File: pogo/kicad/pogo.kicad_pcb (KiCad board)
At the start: 2 copper layers, 7.6 x 15.1 mm, 6 parts

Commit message: Tweaked the layout.
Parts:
- added REF**: SolderJumper, pogo:SolderJumper, F.Cu at (0.00, 3.56)
- moved REF** 2.54 mm to (2.54, 0.00)
- moved REF** 2.54 mm to (0.00, 7.82)
- moved REF** 2.54 mm to (0.00, 0.00)
- moved REF** 2.54 mm to (-2.54, 0.00)
- moved REF** 2.54 mm to (0.00, -2.54)
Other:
- board size 7.6 x 15.1 mm -> 7.9 x 14.9 mm
- board text added: "+"
- board text added: "GND"
- board text added: "POGO PINS THIS SIDE"
- board text added: "SCL"
- board text added: "SDA"
- board text added: "SH 1MM SMD"
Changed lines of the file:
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@@
   (net 0 "")
   (footprint "pogo:POGO_PAD2" (layer "F.Cu")
-    (at 5.08 0)
+    (at 2.54 0)
     (descr "Through hole straight pin header, 1x01, 2.54mm pitch, single row")
     (tags "Through hole pin header THT 1x01 2.54mm single row")
@@
   )
   (footprint "pogo:JST_SH_SM04B-SRSS-TB_1x04-1MP_P1.00mm_Horizontal" (layer "F.Cu")
-    (at 2.54 7.8232)
+    (at 0 7.8232)
     (descr "JST SH series connector, SM04B-SRSS-TB (http://www.jst-mfg.com/product/pdf/eng/eSH.pdf), generated with kicad-footprint-generator")
     (tags "connector JST SH top entry")
@@
   )
   (footprint "pogo:POGO_PAD2" (layer "F.Cu")
-    (at 2.54 0)
+    (at 0 0)
     (descr "Through hole straight pin header, 1x01, 2.54mm pitch, single row")
     (tags "Through hole pin header THT 1x01 2.54mm single row")
@@
   )
   (footprint "pogo:POGO_PAD2" (layer "F.Cu")
-    (at 0 0)
+    (at -2.54 0)
     (descr "Through hole straight pin header, 1x01, 2.54mm pitch, single row")
     (tags "Through hole pin header THT 1x01 2.54mm single row")
@@
     )
   )
-  (footprint "pogo:POGO_PAD2" (layer "F.Cu")
-    (at 2.54 -2.54)
+  (footprint "pogo:SolderJumper" (layer "F.Cu")
+    (at 0 3.556)
+    (descr "SMD Solder Jumper, 1x1.5mm Pads, 0.3mm gap, open")
+    (tags "solder jumper open")
+    (attr exclude_from_pos_files exclude_from_bom)
+    (fp_text reference "REF**" (at 0 -1.8) (layer "F.SilkS") hide
+        (effects (font (size 1 1) (thickness 0.15)))
+    )
+    (fp_text value "SolderJumper" (at 0 1.9) (layer "F.Fab") hide
+        (effects (font (size 1 1) (thickness 0.15)))
+    )
+    (fp_line (start -1.4 -1) (end 1.4 -1)
+      (stroke (width 0.12) (type solid)) (layer "F.SilkS"))
+    (fp_line (start -1.4 1) (end -1.4 -1)
+      (stroke (width 0.12) (type solid)) (layer "F.SilkS"))
+    (fp_line (start 1.4 -1) (end 1.4 1)
+      (stroke (width 0.12) (type solid)) (layer "F.SilkS"))
+    (fp_line (start 1.4 1) (end -1.4 1)
+      (stroke (width 0.12) (type solid)) (layer "F.SilkS"))
+    (pad "1" smd rect (at -0.65 0) (size 1 1.5) (layers "F.Cu" "F.Mask"))
+    (pad "2" smd rect (at 0.65 0) (size 1 1.5) (layers "F.Cu" "F.Mask"))
+  )
+  (footprint "pogo:POGO_PAD2" (layer "F.Cu")
+    (at 0 -2.54)
     (descr "Through hole straight pin header, 1x01, 2.54mm pitch, single row")
     (tags "Through hole pin header THT 1x01 2.54mm single row")
@@
     )
   )
-  (gr_circle (center 0 0) (end 1.27 0)
-    (stroke (width 0.0254) (type default)) (fill none) (layer "F.SilkS"))
-  (gr_circle (center 5.08 0) (end 6.35 0)
-    (stroke (width 0.0254) (type default)) (fill none) (layer "F.SilkS"))
-  (gr_circle (center 2.54 -2.54) (end 3.81 -2.54)
-    (stroke (width 0.0254) (type default)) (fill none) (layer "F.SilkS"))
-  (gr_line (start 6.35 10.7188) (end 6.35 -0.5334)
-    (stroke (width 0.0254) (type default)) (layer "Edge.Cuts"))
-  (gr_line (start 6.35 -0.5334) (end 2.54 -4.3434)
-    (stroke (width 0.0254) (type default)) (layer "Edge.Cuts"))
-  (gr_line (start -1.27 10.7188) (end -1.27 -0.5334)
-    (stroke (width 0.0254) (type default)) (layer "Edge.Cuts"))
-  (gr_line (start -1.27 -0.5334) (end 2.54 -4.3434)
-    (stroke (width 0.0254) (type default)) (layer "Edge.Cuts"))
-  (gr_line (start -1.27 10.7188) (end 6.35 10.7188)
-    (stroke (width 0.0254) (type default)) (layer "Edge.Cuts"))
-  (segment (start 3.81 2.5654) (end 2.04 4.3354) (width 0.4064) (layer "F.Cu") (net 0))
-  (segment (start 2.04 4.3354) (end 2.04 5.62) (width 0.4064) (layer "F.Cu") (net 0))
-  (segment (start 4.04 5.62) (end 4.04 4.0626) (width 0.254) (layer "F.Cu") (net 0))
-  (segment (start 4.04 4.0626) (end 5.08 3.0226) (width 0.254) (layer "F.Cu") (net 0))
-  (segment (start 3.048 5.8312) (end 3.048 6.858) (width 0.254) (layer "F.Cu") (net 0))
-  (segment (start 3.81 2.5654) (end 3.81 -1.27) (width 0.4064) (layer "F.Cu") (net 0))
-  (segment (start 3.81 -1.27) (end 2.54 -2.54) (width 0.4064) (layer "F.Cu") (net 0))
-  (segment (start 0 6.7564) (end 0 0) (width 0.254) (layer "F.Cu") (net 0))
-  (segment (start 1.04 5.62) (end 1.04 1.5762) (width 0.4064) (layer "F.Cu") (net 0))
-  (segment (start 3.048 6.8834) (end 2.6162 7.3152) (width 0.254) (layer "F.Cu") (net 0))
-  (segment (start 5.08 3.0226) (end 5.08 0) (width 0.254) (layer "F.Cu") (net 0))
-  (segment (start 2.6162 7.3152) (end 0.5588 7.3152) (width 0.254) (layer "F.Cu") (net 0))
-  (segment (start 1.04 1.5762) (end 2.54 0.0762) (width 0.4064) (layer "F.Cu") (net 0))
-  (segment (start 0.5588 7.3152) (end 0 6.7564) (width 0.254) (layer "F.Cu") (net 0))
-  (segment (start 2.54 0.0762) (end 2.54 0) (width 0.4064) (layer "F.Cu") (net 0))
+  (gr_line (start 3.937 10.287) (end 3.937 -0.056344)
+    (stroke (width 0.0254) (type default)) (layer "Edge.Cuts"))
+  (gr_line (start 3.527828 -1.044172) (end 0.987828 -3.584172)
+    (stroke (width 0.0254) (type default)) (layer "Edge.Cuts"))
+  (gr_arc (start 3.937 10.287) (mid 3.751013 10.736013) (end 3.302 10.922)
+    (stroke (width 0.0254) (type default)) (layer "Edge.Cuts"))
+  (gr_arc (start -0.987828 -3.584172) (mid 0 -3.993344) (end 0.987828 -3.584172)
+    (stroke (width 0.0254) (type default)) (layer "Edge.Cuts"))
+  (gr_line (start -3.937 10.287) (end -3.937 -0.056344)
+    (stroke (width 0.0254) (type default)) (layer "Edge.Cuts"))
+  (gr_arc (start 3.527828 -1.044172) (mid 3.830659 -0.590953) (end 3.937 -0.056344)
+    (stroke (width 0.0254) (type default)) (layer "Edge.Cuts"))
+  (gr_arc (start -3.937 -0.056344) (mid -3.83066 -0.590953) (end -3.527828 -1.044172)
+    (stroke (width 0.0254) (type default)) (layer "Edge.Cuts"))
+  (gr_line (start -3.527828 -1.044172) (end -0.987828 -3.584172)
+    (stroke (width 0.0254) (type default)) (layer "Edge.Cuts"))
+  (gr_arc (start -3.302 10.922) (mid -3.751013 10.736013) (end -3.937 10.287)
+    (stroke (width 0.0254) (type default)) (layer "Edge.Cuts"))
+  (gr_line (start -3.302 10.922) (end 3.302 10.922)
+    (stroke (width 0.0254) (type default)) (layer "Edge.Cuts"))
+  (gr_text "POGO PINS\nTHIS SIDE" (at 0 2.413) (layer "B.SilkS")
+    (effects (font (size 0.75 0.75) (thickness 0.15)) (justify top mirror))
+  )
+  (gr_text "SCL" (at 2.54 1.016) (layer "F.SilkS")
+    (effects (font (size 0.75 0.75) (thickness 0.15)) (justify top))
+  )
+  (gr_text "+" (at -1.27 -2.667) (layer "F.SilkS")
+    (effects (font (size 0.75 0.75) (thickness 0.15)) (justify top))
+  )
+  (gr_text "GND" (at 0 1.016) (layer "F.SilkS")
+    (effects (font (size 0.75 0.75) (thickness 0.15)) (justify top))
+  )
+  (gr_text "SH 1MM\nSMD" (at 0 7.239) (layer "F.SilkS")
+    (effects (font (size 0.75 0.75) (thickness 0.15)) (justify top))
+  )
+  (gr_text "SDA" (at -2.54 1.016) (layer "F.SilkS")
+    (effects (font (size 0.75 0.75) (thickness 0.15)) (justify top))
+  )
+  (segment (start 0.65 1.763) (end 1.27 1.143) (width 0.4064) (layer "F.Cu") (net 0))
+  (segment (start 1.27 1.143) (end 1.27 -1.27) (width 0.4064) (layer "F.Cu") (net 0))
+  (segment (start 0.508 6.8834) (end -0.1016 7.493) (width 0.254) (layer "F.Cu") (net 0))
+  (segment (start -0.65 3.175) (end -0.5 3.325) (width 0.4064) (layer "F.Cu") (net 0))
+  (segment (start -2.794 6.731) (end -2.794 1.651) (width 0.254) (layer "F.Cu") (net 0))
+  (segment (start -0.5 3.325) (end -0.5 5.62) (width 0.4064) (layer "F.Cu") (net 0))
+  (segment (start 0.508 5.8312) (end 0.508 6.858) (width 0.254) (layer "F.Cu") (net 0))
+  (segment (start -2.032 7.493) (end -2.794 6.731) (width 0.254) (layer "F.Cu") (net 0))
+  (segment (start 0.65 3.175) (end 0.65 1.763) (width 0.4064) (layer "F.Cu") (net 0))
+  (segment (start -2.54 1.397) (end -2.54 0) (width 0.254) (layer "F.Cu") (net 0))
+  (segment (start 1.27 -1.27) (end 0 -2.54) (width 0.4064) (layer "F.Cu") (net 0))
+  (segment (start -2.794 1.651) (end -2.54 1.397) (width 0.254) (layer "F.Cu") (net 0))
+  (segment (start -1.5 5.62) (end -1.5 4.85) (width 0.4064) (layer "F.Cu") (net 0))
+  (segment (start -1.905 4.445) (end -1.905 1.905) (width 0.4064) (layer "F.Cu") (net 0))
+  (segment (start 2.54 3.81) (end 2.54 0) (width 0.254) (layer "F.Cu") (net 0))
+  (segment (start -1.5 4.85) (end -1.905 4.445) (width 0.4064) (layer "F.Cu") (net 0))
+  (segment (start -0.1016 7.493) (end -2.032 7.493) (width 0.254) (layer "F.Cu") (net 0))
+  (segment (start 1.5 5.62) (end 1.5 4.85) (width 0.254) (layer "F.Cu") (net 0))
+  (segment (start 1.5 4.85) (end 2.54 3.81) (width 0.254) (layer "F.Cu") (net 0))
+  (segment (start -1.905 1.905) (end 0 0) (width 0.4064) (layer "F.Cu") (net 0))
 )

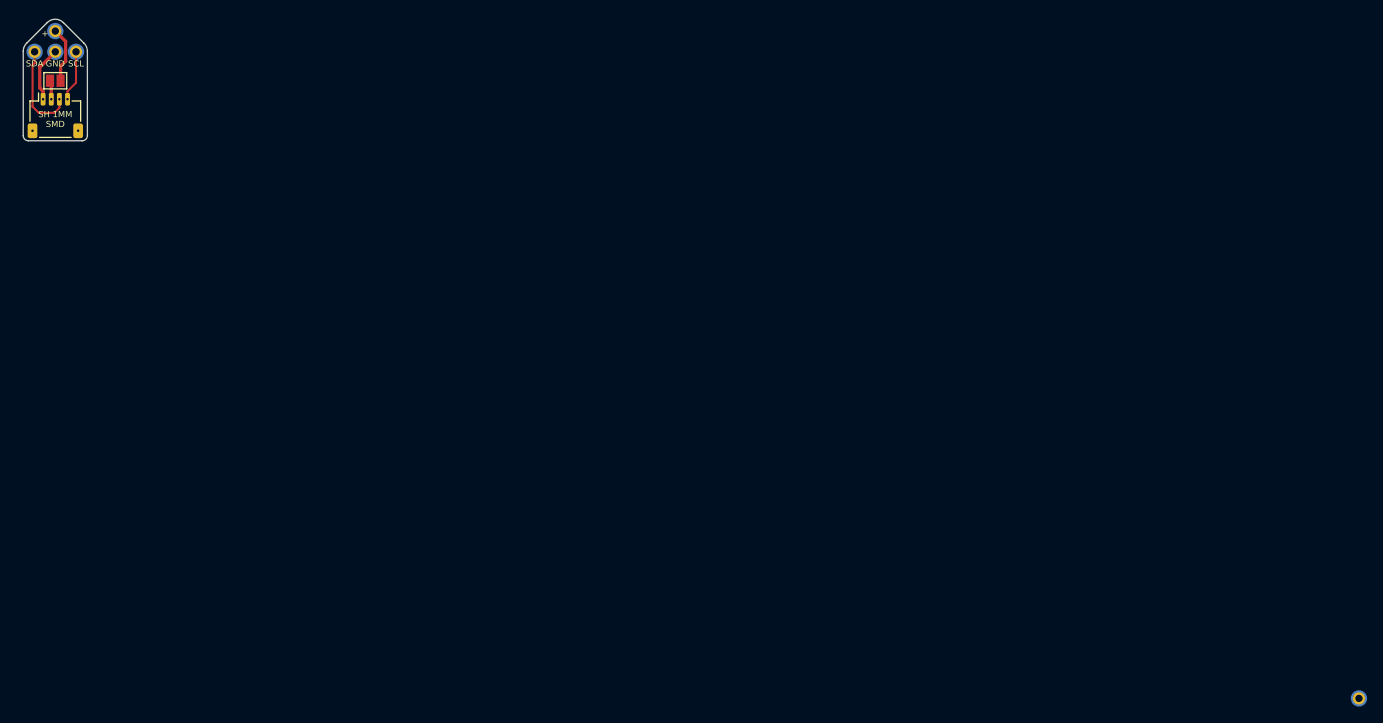
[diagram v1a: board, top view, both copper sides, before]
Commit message: More tweakes to the POGO design. Also, added a socket footprint.
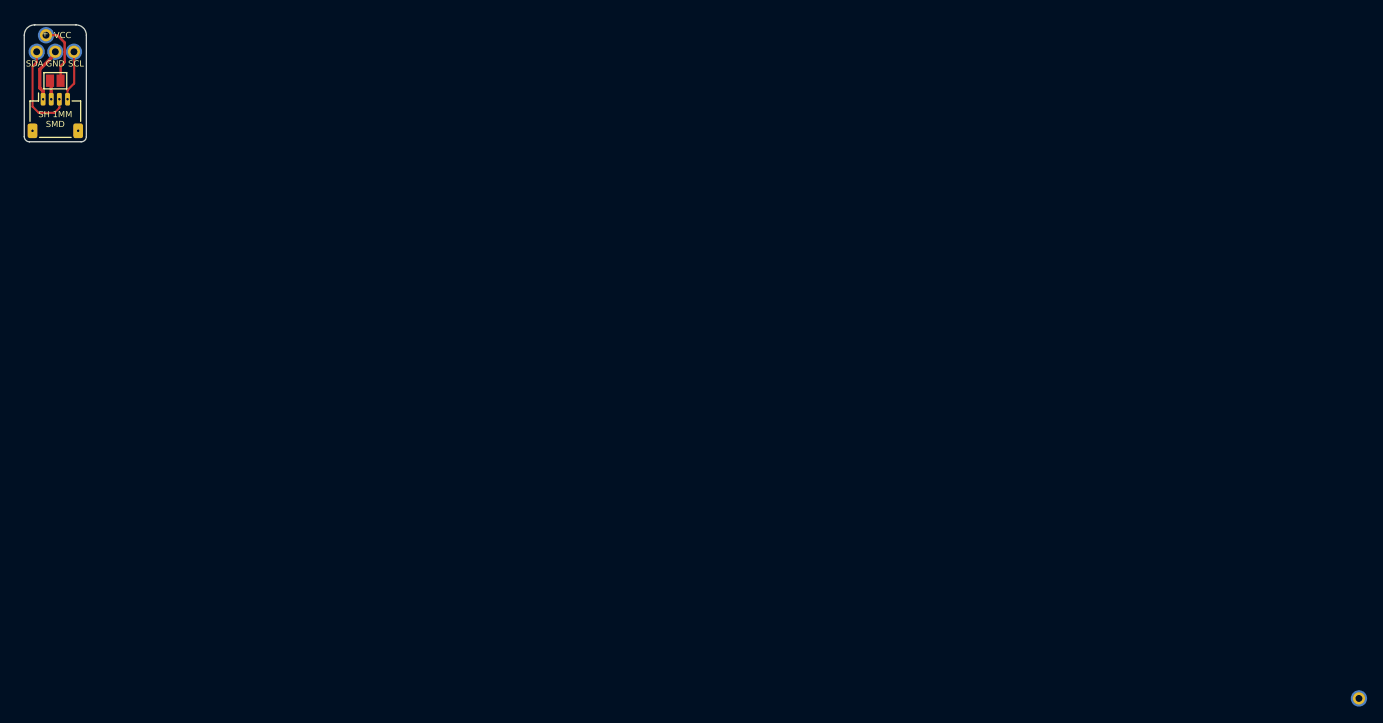
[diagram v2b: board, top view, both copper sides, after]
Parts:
- REF** (x5): value POGO_PAD2 -> POGO_PIN; footprint pogo:POGO_PAD2 -> pogo:POGO_PIN
- REF**: value SolderJumper -> SOLDER_JUMPER; footprint pogo:SolderJumper -> pogo:SOLDER_JUMPER
- moved REF** 2.54 mm to (0.00, 0.00)
- moved REF** 2.33 mm to (-1.14, -2.03)
- moved REF** 0.25 mm to (2.29, 0.00)
- moved REF** 0.25 mm to (-2.29, 0.00)
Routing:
- net (no net): track 33.4 -> 34.1 mm
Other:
- board size 7.9 x 14.9 mm -> 7.6 x 14.4 mm
- board text added: "VCC"
